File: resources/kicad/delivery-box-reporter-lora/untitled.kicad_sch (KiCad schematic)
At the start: 2 parts, among them U7 WeMos_D1_mini

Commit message: Mostly changes to the box and board design
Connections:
- net 3v3B: now also U8.5 (3.3v); no longer U8.1 (3.3v)
- net SS RX: now also U8.2 (TX); no longer U8.4 (TX)
- net at U7.10 (GND): now also U8.1 (GND); no longer U8.5 (GND)

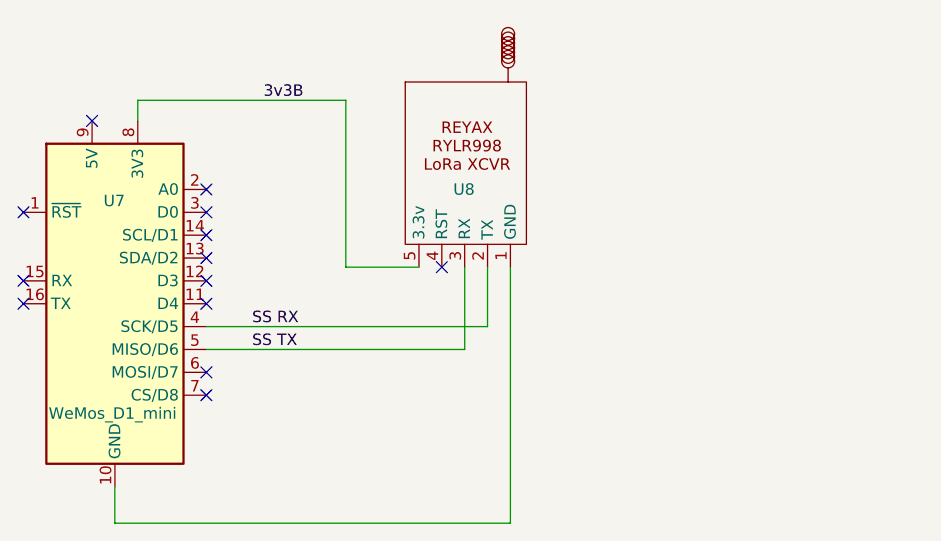
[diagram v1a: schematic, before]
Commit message: Changes to the enclosures, presentation, and code
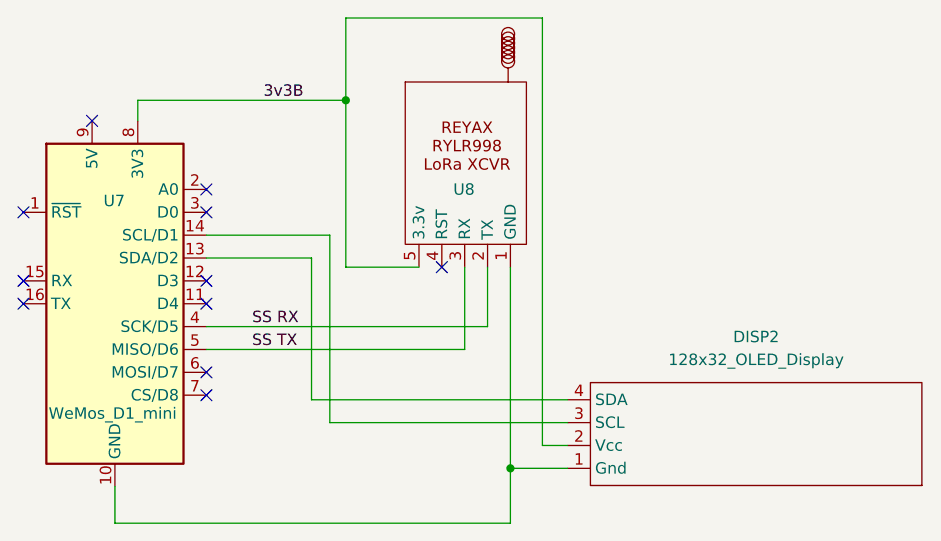
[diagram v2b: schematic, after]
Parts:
- added DISP2: 128x32_OLED_Display, Davids_Footprints:OLED_0.91_128x32, symbol Davids_Symbols:128x32_OLED_Display
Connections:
- net 3v3B: now also DISP2.2 (Vcc)
- net at U7.10 (GND), U8.1 (GND): now also DISP2.1 (Gnd)
- net at U7.13 (SDA/D2): now also DISP2.4 (SDA)
- net at U7.14 (SCL/D1): now also DISP2.3 (SCL)
- no-connect marks 13 -> 11
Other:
- title: (none) -> LoRa to MQTT Converter
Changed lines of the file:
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@@
 	(generator_version "8.0")
 	(paper "A4")
-	(no_connect
-		(at 134.112 74.93)
+	(title_block
+		(title "LoRa to MQTT Converter")
+		(date "2025-02-08")
+		(rev "2.2.0")
+	)
+	(junction
+		(at 149.606 59.944)
+		(diameter 0)
+		(color 0 0 0 0)
+	)
+	(junction
+		(at 167.894 100.838)
+		(diameter 0)
+		(color 0 0 0 0)
 	)
 	(no_connect
@@
 	)
 	(no_connect
-		(at 134.112 77.47)
-	)
-	(no_connect
 		(at 121.412 62.23)
 	)
@@
 	(wire
 		(pts
+			(xy 174.244 93.218) (xy 145.796 93.218)
+		)
+		(stroke
+			(width 0)
+			(type default)
+		)
+	)
+	(wire
+		(pts
+			(xy 147.828 95.758) (xy 147.828 74.93)
+		)
+		(stroke
+			(width 0)
+			(type default)
+		)
+	)
+	(wire
+		(pts
+			(xy 149.606 50.8) (xy 149.606 59.944)
+		)
+		(stroke
+			(width 0)
+			(type default)
+		)
+	)
+	(wire
+		(pts
 			(xy 167.894 106.934) (xy 123.952 106.934)
 		)
@@
 	(wire
 		(pts
+			(xy 174.244 95.758) (xy 147.828 95.758)
+		)
+		(stroke
+			(width 0)
+			(type default)
+		)
+	)
+	(wire
+		(pts
 			(xy 157.734 78.486) (xy 149.606 78.486)
 		)
@@
 	(wire
 		(pts
-			(xy 167.894 78.486) (xy 167.894 106.934)
+			(xy 171.45 98.298) (xy 171.45 50.8)
+		)
+		(stroke
+			(width 0)
+			(type default)
+		)
+	)
+	(wire
+		(pts
+			(xy 167.894 78.486) (xy 167.894 100.838)
 		)
 		(stroke
@@
 	(wire
 		(pts
+			(xy 145.796 77.47) (xy 134.112 77.47)
+		)
+		(stroke
+			(width 0)
+			(type default)
+		)
+	)
+	(wire
+		(pts
 			(xy 134.112 87.63) (xy 162.814 87.63)
 		)
@@
 	(wire
 		(pts
+			(xy 167.894 100.838) (xy 174.244 100.838)
+		)
+		(stroke
+			(width 0)
+			(type default)
+		)
+	)
+	(wire
+		(pts
+			(xy 174.244 98.298) (xy 171.45 98.298)
+		)
+		(stroke
+			(width 0)
+			(type default)
+		)
+	)
+	(wire
+		(pts
 			(xy 126.492 59.944) (xy 126.492 62.23)
 		)
@@
 	(wire
 		(pts
+			(xy 147.828 74.93) (xy 134.112 74.93)
+		)
+		(stroke
+			(width 0)
+			(type default)
+		)
+	)
+	(wire
+		(pts
 			(xy 134.112 85.09) (xy 165.354 85.09)
+		)
+		(stroke
+			(width 0)
+			(type default)
+		)
+	)
+	(wire
+		(pts
+			(xy 145.796 93.218) (xy 145.796 77.47)
+		)
+		(stroke
+			(width 0)
+			(type default)
+		)
+	)
+	(wire
+		(pts
+			(xy 167.894 100.838) (xy 167.894 106.934)
+		)
+		(stroke
+			(width 0)
+			(type default)
+		)
+	)
+	(wire
+		(pts
+			(xy 171.45 50.8) (xy 149.606 50.8)
 		)
 		(stroke
@@
 		)
 	)
+	(symbol
+		(lib_id "Davids_Symbols:128x32_OLED_Display")
+		(at 187.579 90.043 0)
+		(unit 1)
+		(exclude_from_sim no)
+		(in_bom yes)
+		(on_board yes)
+		(dnp no)
+		(fields_autoplaced yes)
+		(property "Reference" "DISP2"
+			(at 195.199 86.233 0)
+			(effects
+				(font
+					(size 1.27 1.27)
+				)
+			)
+		)
+		(property "Value" "128x32_OLED_Display"
+			(at 195.199 88.773 0)
+			(effects
+				(font
+					(size 1.27 1.27)
+				)
+			)
+		)
+		(property "Footprint" "Davids_Footprints:OLED_0.91_128x32"
+			(at 195.834 104.013 0)
+			(effects
+				(font
+					(size 1.27 1.27)
+				)
+				(hide yes)
+			)
+		)
+		(property "Datasheet" ""
+			(at 187.579 90.043 0)
+			(effects
+				(font
+					(size 1.27 1.27)
+				)
+				(hide yes)
+			)
+		)
+		(property "Description" ""
+			(at 187.579 90.043 0)
+			(effects
+				(font
+					(size 1.27 1.27)
+				)
+				(hide yes)
+			)
+		)
+		(pin "1"
+		)
+		(pin "4"
+		)
+		(pin "3"
+		)
+		(pin "2"
+		)
+		(instances
+			(project "delivery-box-reporter-lora"
+				(path "/b5a49f66-f3e1-4174-95b7-6fa32f14e918/4cbaa3c5-96cf-4434-b6fb-bcb8497e150b"
+					(reference "DISP2")
+					(unit 1)
+				)
+			)
+		)
+	)
